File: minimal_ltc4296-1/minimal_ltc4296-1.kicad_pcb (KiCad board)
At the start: 2 copper layers, 15.2 x 15.2 mm, 1 part, among them U1 LTC4296AUK-1-PBF

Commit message: Update KiCad project files
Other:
- copper layers 2 -> 4
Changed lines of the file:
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@@
 	(layers
 		(0 "F.Cu" signal)
+		(4 "In1.Cu" power)
+		(6 "In2.Cu" power)
 		(2 "B.Cu" signal)
 		(9 "F.Adhes" user "F.Adhesive")
@@
 		(43 "User.3" user)
 		(45 "User.4" user)
+		(47 "User.5" user)
+		(49 "User.6" user)
+		(51 "User.7" user)
+		(53 "User.8" user)
+		(55 "User.9" user)
 	)
 	(setup
+		(stackup
+			(layer "F.SilkS"
+				(type "Top Silk Screen")
+				(color "White")
+				(material "Direct Printing")
+			)
+			(layer "F.Paste"
+				(type "Top Solder Paste")
+			)
+			(layer "F.Mask"
+				(type "Top Solder Mask")
+				(color "Green")
+				(thickness 0.01)
+				(material "Epoxy")
+				(epsilon_r 3.3)
+				(loss_tangent 0)
+			)
+			(layer "F.Cu"
+				(type "copper")
+				(thickness 0.035)
+			)
+			(layer "dielectric 1"
+				(type "prepreg")
+				(color "FR4 natural")
+				(thickness 0.1)
+				(material "FR4")
+				(epsilon_r 4.5)
+				(loss_tangent 0.02)
+			)
+			(layer "In1.Cu"
+				(type "copper")
+				(thickness 0.035)
+			)
+			(layer "dielectric 2"
+				(type "core")
+				(color "FR4 natural")
+				(thickness 1.24)
+				(material "FR4")
+				(epsilon_r 4.5)
+				(loss_tangent 0.02)
+			)
+			(layer "In2.Cu"
+				(type "copper")
+				(thickness 0.035)
+			)
+			(layer "dielectric 3"
+				(type "prepreg")
+				(color "FR4 natural")
+				(thickness 0.1)
+				(material "FR4")
+				(epsilon_r 4.5)
+				(loss_tangent 0.02)
+			)
+			(layer "B.Cu"
+				(type "copper")
+				(thickness 0.035)
+			)
+			(layer "B.Mask"
+				(type "Bottom Solder Mask")
+				(color "Green")
+				(thickness 0.01)
+				(material "Epoxy")
+				(epsilon_r 3.3)
+				(loss_tangent 0)
+			)
+			(layer "B.Paste"
+				(type "Bottom Solder Paste")
+			)
+			(layer "B.SilkS"
+				(type "Bottom Silk Screen")
+				(color "White")
+				(material "Direct Printing")
+			)
+			(copper_finish "Immersion gold")
+			(dielectric_constraints yes)
+			(edge_connector yes)
+		)
 		(pad_to_mask_clearance 0)
 		(allow_soldermask_bridges_in_footprints no)

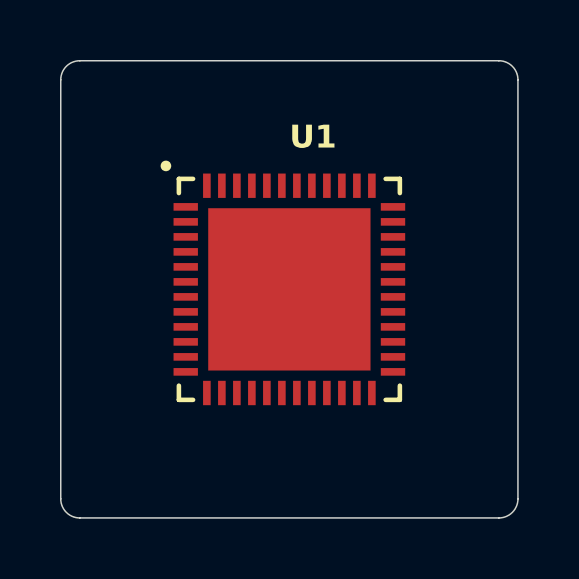
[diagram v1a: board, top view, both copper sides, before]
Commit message: Update KiCAD project files and generator
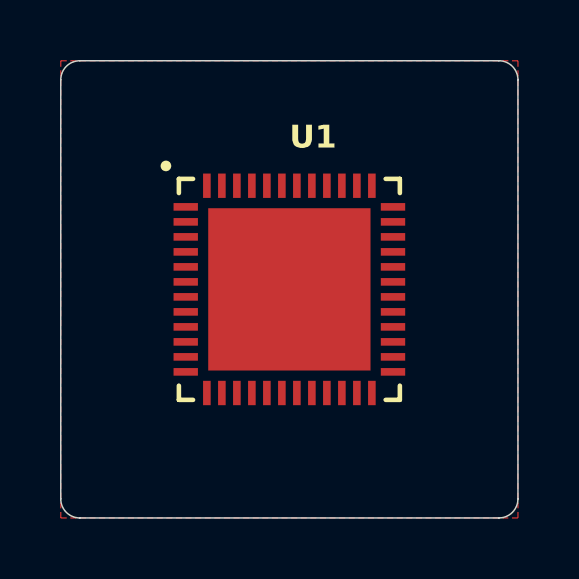
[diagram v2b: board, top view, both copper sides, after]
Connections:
- U1 pad 21: unconnected-(U1-GND-Pad21) -> GND
- U1 pad 24: unconnected-(U1-LSRC-Pad24) -> GND
- U1 pad 49: unconnected-(U1-GND-Pad49) -> GND
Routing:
- added copper zone on F.Cu, net GND
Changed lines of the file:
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@@
 	(net 11 "unconnected-(U1-LSNS1{slash}LSNS2-Pad28)")
 	(net 12 "unconnected-(U1-SW3-Pad19)")
-	(net 13 "unconnected-(U1-LSRC-Pad24)")
+	(net 13 "GND")
 	(net 14 "unconnected-(U1-HSNSP1-Pad48)")
 	(net 15 "unconnected-(U1-HSNSM2-Pad43)")
@@
 	(net 21 "unconnected-(U1-SW4-Pad20)")
 	(net 22 "unconnected-(U1-CPO-Pad7)")
-	(net 23 "unconnected-(U1-*CS-Pad12)")
+	(net 23 "unconnected-(U1-~{CS}-Pad12)")
 	(net 24 "unconnected-(U1-SW0-Pad16)")
 	(net 25 "unconnected-(U1-LSNS3{slash}LSNS4-Pad31)")
@@
 	(net 35 "unconnected-(U1-RT-Pad22)")
 	(net 36 "unconnected-(U1-OUTP0-Pad1)")
-	(net 37 "unconnected-(U1-GND-Pad49)")
-	(net 38 "unconnected-(U1-GND-Pad21)")
-	(net 39 "unconnected-(U1-HSNSM1-Pad47)")
-	(net 40 "unconnected-(U1-OUTP1-Pad45)")
-	(net 41 "unconnected-(U1-HGATE4-Pad34)")
-	(net 42 "unconnected-(U1-OUTM4-Pad32)")
-	(net 43 "unconnected-(U1-AUTO-Pad13)")
-	(net 44 "unconnected-(U1-SW2-Pad18)")
-	(net 45 "unconnected-(U1-HSNSM4-Pad35)")
-	(net 46 "unconnected-(U1-OUTM0-Pad25)")
-	(net 47 "unconnected-(U1-HSNSP2-Pad44)")
-	(net 48 "unconnected-(U1-HSNSM3-Pad39)")
-	(net 49 "unconnected-(U1-OUTP2-Pad41)")
+	(net 37 "unconnected-(U1-HSNSM1-Pad47)")
+	(net 38 "unconnected-(U1-OUTP1-Pad45)")
+	(net 39 "unconnected-(U1-HGATE4-Pad34)")
+	(net 40 "unconnected-(U1-OUTM4-Pad32)")
+	(net 41 "unconnected-(U1-AUTO-Pad13)")
+	(net 42 "unconnected-(U1-SW2-Pad18)")
+	(net 43 "unconnected-(U1-HSNSM4-Pad35)")
+	(net 44 "unconnected-(U1-OUTM0-Pad25)")
+	(net 45 "unconnected-(U1-HSNSP2-Pad44)")
+	(net 46 "unconnected-(U1-HSNSM3-Pad39)")
+	(net 47 "unconnected-(U1-OUTP2-Pad41)")
 	(footprint "analog_devices_footprints:QFN48_05-08-7073_ADI"
 		(layer "F.Cu")
@@
 			(size 0.254 0.8128)
 			(layers "F.Cu" "F.Mask" "F.Paste")
-			(net 23 "unconnected-(U1-*CS-Pad12)")
-			(pinfunction "*CS")
+			(net 23 "unconnected-(U1-~{CS}-Pad12)")
+			(pinfunction "~{CS}")
 			(pintype "input")
 		)
@@
 			(size 0.254 0.8128)
 			(layers "F.Cu" "F.Mask" "F.Paste")
-			(net 43 "unconnected-(U1-AUTO-Pad13)")
+			(net 41 "unconnected-(U1-AUTO-Pad13)")
 			(pinfunction "AUTO")
 			(pintype "unspecified")
@@
 			(size 0.254 0.8128)
 			(layers "F.Cu" "F.Mask" "F.Paste")
-			(net 44 "unconnected-(U1-SW2-Pad18)")
+			(net 42 "unconnected-(U1-SW2-Pad18)")
 			(pinfunction "SW2")
 			(pintype "output")
@@
 			(size 0.254 0.8128)
 			(layers "F.Cu" "F.Mask" "F.Paste")
-			(net 38 "unconnected-(U1-GND-Pad21)")
+			(net 13 "GND")
 			(pinfunction "GND")
 			(pintype "power_out")
@@
 			(size 0.254 0.8128)
 			(layers "F.Cu" "F.Mask" "F.Paste")
-			(net 13 "unconnected-(U1-LSRC-Pad24)")
+			(net 13 "GND")
 			(pinfunction "LSRC")
 			(pintype "unspecified")
@@
 			(size 0.254 0.8128)
 			(layers "F.Cu" "F.Mask" "F.Paste")
-			(net 46 "unconnected-(U1-OUTM0-Pad25)")
+			(net 44 "unconnected-(U1-OUTM0-Pad25)")
 			(pinfunction "OUTM0")
 			(pintype "output")
@@
 			(size 0.254 0.8128)
 			(layers "F.Cu" "F.Mask" "F.Paste")
-			(net 42 "unconnected-(U1-OUTM4-Pad32)")
+			(net 40 "unconnected-(U1-OUTM4-Pad32)")
 			(pinfunction "OUTM4")
 			(pintype "output")
@@
 			(size 0.254 0.8128)
 			(layers "F.Cu" "F.Mask" "F.Paste")
-			(net 41 "unconnected-(U1-HGATE4-Pad34)")
+			(net 39 "unconnected-(U1-HGATE4-Pad34)")
 			(pinfunction "HGATE4")
 			(pintype "unspecified")
@@
 			(size 0.254 0.8128)
 			(layers "F.Cu" "F.Mask" "F.Paste")
-			(net 45 "unconnected-(U1-HSNSM4-Pad35)")
+			(net 43 "unconnected-(U1-HSNSM4-Pad35)")
 			(pinfunction "HSNSM4")
 			(pintype "input")
@@
 			(size 0.254 0.8128)
 			(layers "F.Cu" "F.Mask" "F.Paste")
-			(net 48 "unconnected-(U1-HSNSM3-Pad39)")
+			(net 46 "unconnected-(U1-HSNSM3-Pad39)")
 			(pinfunction "HSNSM3")
 			(pintype "input")
@@
 			(size 0.254 0.8128)
 			(layers "F.Cu" "F.Mask" "F.Paste")
-			(net 49 "unconnected-(U1-OUTP2-Pad41)")
+			(net 47 "unconnected-(U1-OUTP2-Pad41)")
 			(pinfunction "OUTP2")
 			(pintype "output")
@@
 			(size 0.254 0.8128)
 			(layers "F.Cu" "F.Mask" "F.Paste")
-			(net 47 "unconnected-(U1-HSNSP2-Pad44)")
+			(net 45 "unconnected-(U1-HSNSP2-Pad44)")
 			(pinfunction "HSNSP2")
 			(pintype "input")
@@
 			(size 0.254 0.8128)
 			(layers "F.Cu" "F.Mask" "F.Paste")
-			(net 40 "unconnected-(U1-OUTP1-Pad45)")
+			(net 38 "unconnected-(U1-OUTP1-Pad45)")
 			(pinfunction "OUTP1")
 			(pintype "output")
@@
 			(size 0.254 0.8128)
 			(layers "F.Cu" "F.Mask" "F.Paste")
-			(net 39 "unconnected-(U1-HSNSM1-Pad47)")
+			(net 37 "unconnected-(U1-HSNSM1-Pad47)")
 			(pinfunction "HSNSM1")
 			(pintype "input")
@@
 			(size 5.4102 5.4102)
 			(layers "F.Cu" "F.Mask" "F.Paste")
-			(net 37 "unconnected-(U1-GND-Pad49)")
+			(net 13 "GND")
 			(pinfunction "GND")
 			(pintype "power_out")
+			(zone_connect 2)
 		)
 		(embedded_fonts no)
@@
 		(layer "Edge.Cuts")
 	)
+	(zone
+		(net 13)
+		(net_name "GND")
+		(layer "F.Cu")
+		(hatch none 0.508)
+		(connect_pads
+			(clearance 0.2032)
+		)
+		(min_thickness 0.2032)
+		(filled_areas_thickness no)
+		(fill yes
+			(thermal_gap 0.2032)
+			(thermal_bridge_width 0.2032)
+			(smoothing fillet)
+			(radius 0.508)
+		)
+		(polygon
+			(pts
+				(xy 142.0876 94.742) (xy 142.0876 109.982) (xy 157.3276 109.982) (xy 157.3276 94.742)
+			)
+		)
+	)
 	(embedded_fonts no)

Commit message: Update KiCad project files
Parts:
- added C1: 1 nF, capacitor_footprints:C_0402_1005Metric, F.Cu at (144.8, 102.4)
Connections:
- U1 pad 6: unconnected-(U1-IN-Pad6) -> /IN
- U1 pad 7: unconnected-(U1-CPO-Pad7) -> /CPO
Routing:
- net /IN: track 0.00 -> 1.49 mm
- net /CPO: track 0.00 -> 1.49 mm

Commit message: Update KiCAD files and submodule
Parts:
- added C2: 100 nF, capacitor_footprints:C_0603_1608Metric, F.Cu at (143.4, 99.5)
- added C3: 10 µF, capacitor_footprints:C_1210_250_3225Metric, F.Cu at (140.9, 102.0)
- added C4: 470 nF, capacitor_footprints:C_0402_1005Metric, F.Cu at (143.4, 104.2)
- added C5: 100 nF, capacitor_footprints:C_0603_1608Metric, F.Cu at (138.9, 108.6)
- added D1: 58 V, diode_footprints:DO-214AA, F.Cu at (137.0, 103.0)
- added R1: 10 kΩ, resistor_footprints:R_0402_1005Metric, F.Cu at (142.0, 105.9)
- added R2: 4.99 kΩ, resistor_footprints:R_0402_1005Metric, F.Cu at (142.0, 107.2)
- added R3: 10 kΩ, resistor_footprints:R_0402_1005Metric, F.Cu at (142.0, 108.6)
- added R4: 10 kΩ, resistor_footprints:R_0402_1005Metric, F.Cu at (145.4, 108.6)
- moved C1 1.42 mm to (143.4, 102.1)
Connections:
- U1 pad 10: unconnected-(U1-SDO-Pad10) -> /SDO
- U1 pad 11: unconnected-(U1-SCK-Pad11) -> /SCK
- U1 pad 12: unconnected-(U1-~{CS}-Pad12) -> /~{CS}
- U1 pad 8: unconnected-(U1-INT-Pad8) -> /INT
- U1 pad 9: unconnected-(U1-SDI-Pad9) -> /SDI
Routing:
- net /SCK: track 0.00 -> 6.48 mm, vias 0 -> 2
- net /SDO: track 0.00 -> 5.79 mm, vias 0 -> 2
- net /~{CS}: track 0.00 -> 5.54 mm, vias 0 -> 2
- net /SDI: track 0.00 -> 5.16 mm, vias 0 -> 2
- net /INT: track 0.00 -> 2.96 mm
- net /IN: track 1.49 -> 0.00 mm, vias 0 -> 8
- net /CPO: track 1.49 -> 2.82 mm
- net GND: vias 0 -> 9
- net /3V3: vias 0 -> 5
- added copper zone on F.Cu, net /3V3
- added copper zone on F.Cu, net /IN
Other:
- board size 15.2 x 15.2 mm -> 25.4 x 17.8 mm

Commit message: Update KiCAD files and submodule
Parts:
- added R5: 100 kΩ, resistor_footprints:R_0402_1005Metric, F.Cu at (147.2, 109.7)
- added R6: 100 kΩ, resistor_footprints:R_0402_1005Metric, F.Cu at (148.6, 109.7)
- moved R1 3.79 mm to (142.0, 109.7), turned to 90 degrees
- moved R3 2.80 mm to (144.6, 109.7), turned to 90 degrees
- moved R2 2.76 mm to (143.3, 109.7), turned to 90 degrees
- moved C5 1.91 mm to (140.4, 109.7), turned to 90 degrees
- moved R4 1.29 mm to (145.9, 109.7), turned to 90 degrees
- moved D1 0.25 mm to (136.8, 103.0)
- moved C3 0.25 mm to (140.6, 102.0)
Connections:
- U1 pad 13: unconnected-(U1-AUTO-Pad13) -> /AUTO
- U1 pad 14: unconnected-(U1-WAKEUP-Pad14) -> /WAKEUP
- U1 pad 16: unconnected-(U1-SW0-Pad16) -> /SW0
- U1 pad 17: unconnected-(U1-SW1-Pad17) -> /SW1
- U1 pad 18: unconnected-(U1-SW2-Pad18) -> /SW2
- U1 pad 19: unconnected-(U1-SW3-Pad19) -> /SW3
- U1 pad 20: unconnected-(U1-SW4-Pad20) -> /SW4
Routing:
- net /AUTO: track 0.00 -> 4.91 mm, vias 0 -> 2
- net /SDI: track 5.16 -> 8.24 mm
- net /SW2: track 0.00 -> 2.16 mm, vias 0 -> 1
- net /SW3: track 0.00 -> 1.67 mm, vias 0 -> 1
- net /SW1: track 0.00 -> 1.67 mm, vias 0 -> 1
- net /SDO: track 5.79 -> 7.01 mm
- net /SW0: track 0.00 -> 1.17 mm, vias 0 -> 1
- net /WAKEUP: track 0.00 -> 1.17 mm, vias 0 -> 1
- net /SW4: track 0.00 -> 1.17 mm, vias 0 -> 1
- net /SCK: track 6.48 -> 5.82 mm
- net GND: vias 9 -> 10
- net /3V3: vias 5 -> 6
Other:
- board size 25.4 x 17.8 mm -> 25.4 x 20.3 mm

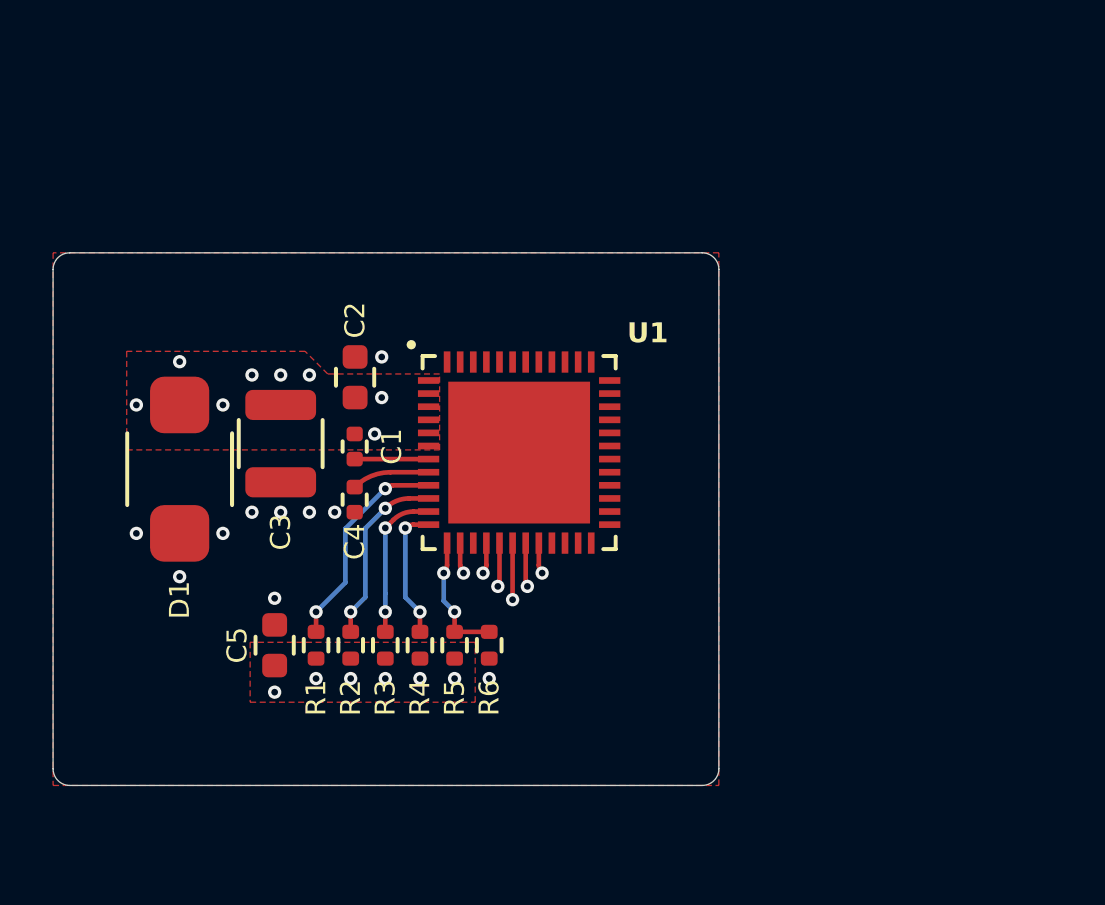
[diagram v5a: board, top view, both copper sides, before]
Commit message: Update KiCAD project files and generator
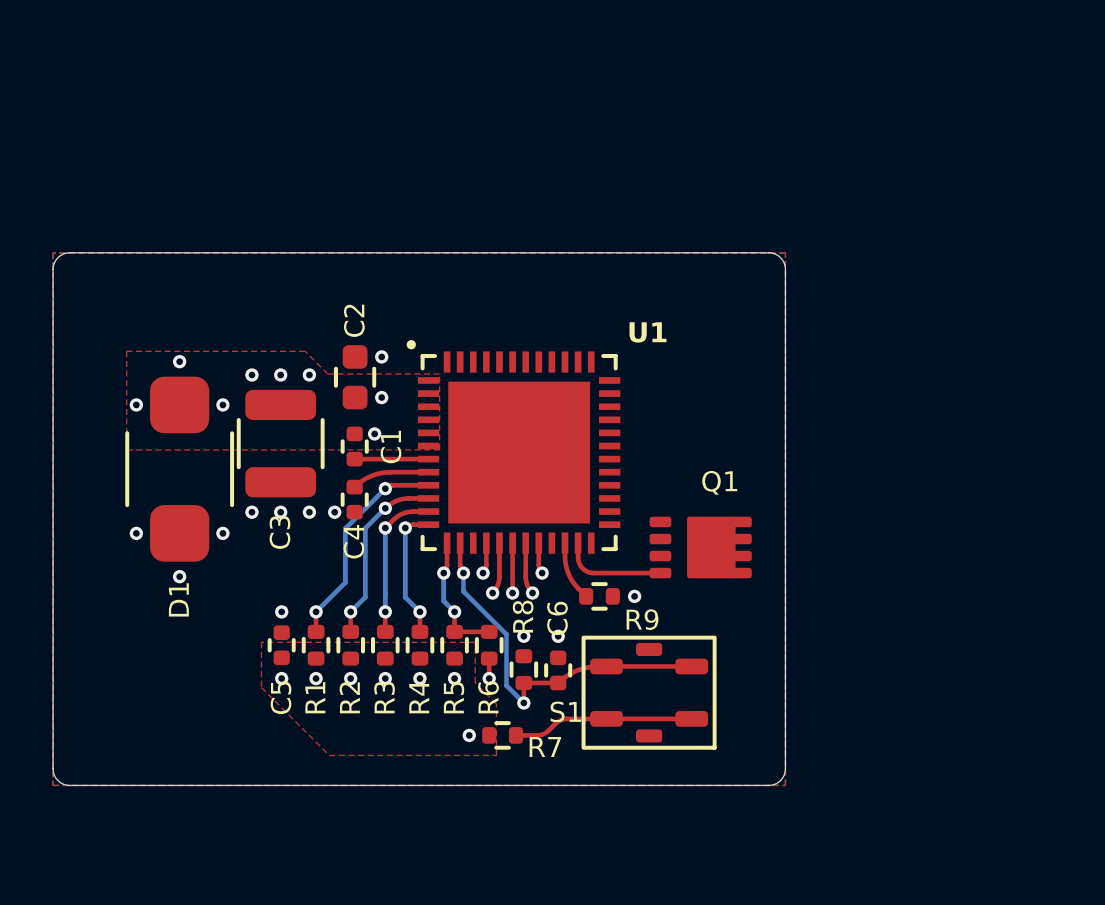
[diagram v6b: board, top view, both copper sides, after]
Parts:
- added C6: 1 nF, capacitor_footprints:C_0402_1005Metric, F.Cu at (151.2, 110.7)
- added Q1: 100.0 V, transistor_footprints:LFPAK33-8, F.Cu at (156.6, 106.0)
- added R7: 1 kΩ, resistor_footprints:R_0402_1005Metric, F.Cu at (149.1, 113.2)
- added R8: 100 kΩ, resistor_footprints:R_0402_1005Metric, F.Cu at (149.9, 110.6)
- added R9: 24.3 kΩ, resistor_footprints:R_0402_1005Metric, F.Cu at (152.8, 107.8)
- added S1: TS21-34-035-BK-160-SMT-TR, tactile_switches_footprints:TS21, F.Cu at (154.7, 111.5)
- C5: value 100 nF -> 1 nF; footprint capacitor_footprints:C_0603_1608Metric -> capacitor_footprints:C_0402_1005Metric
- moved C5 0.27 mm to (140.6, 109.7)
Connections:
- U1 pad 22: unconnected-(U1-RT-Pad22) -> /RT
- U1 pad 23: unconnected-(U1-LGATE-Pad23) -> Net-(Q1-G)
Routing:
- net /WAKEUP: track 1.17 -> 14.4 mm, vias 1 -> 2
- net Net-(R7-Pad2): track 0.00 -> 6.90 mm
- net Net-(Q1-G): track 0.00 -> 4.00 mm
- net /RT: track 0.00 -> 2.28 mm
- net GND: track 0.00 -> 0.76 mm, vias 10 -> 13
- net /3V3: vias 6 -> 7
- added copper zone on In1.Cu, net /3V3
- added copper zone on In1.Cu, net /IN
- added copper zone on B.Cu, net GND
- added copper zone on In1.Cu, net GND
- added copper zone on In2.Cu, net GND
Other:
- board size 25.4 x 20.3 mm -> 27.9 x 20.3 mm

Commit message: Update KiCAD schematic and PCB files
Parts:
- added R10: 24 mΩ, resistor_footprints:R_0612_1632Metric, F.Cu at (163.1, 101.2)
- added R11: 62 mΩ, resistor_footprints:R_0612_1632Metric, F.Cu at (163.1, 97.8)
- added R12: 16 mΩ, resistor_footprints:R_0612_1632Metric, F.Cu at (163.1, 107.9)
- added R13: 62 mΩ, resistor_footprints:R_0612_1632Metric, F.Cu at (163.1, 104.5)
- added R14: 390 mΩ, resistor_footprints:R_0612_1632Metric, F.Cu at (163.1, 111.2)
- moved Q1 2.08 mm to (156.1, 108.0)
- moved R9 0.73 mm to (152.2, 108.2), turned to -90 degrees
- moved S1 0.63 mm to (154.7, 112.2)
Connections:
- Q1 pad 5: unconnected-(Q1-D-Pad5) -> /LSNS
- U1 pad 25: unconnected-(U1-OUTM0-Pad25) -> /OUTM0
- U1 pad 26: unconnected-(U1-LSNS0-Pad26) -> /LSNS
- U1 pad 27: unconnected-(U1-OUTM1-Pad27) -> /OUTM1
- U1 pad 28: unconnected-(U1-LSNS1/LSNS2-Pad28) -> /LSNS
- U1 pad 29: unconnected-(U1-OUTM2-Pad29) -> /OUTM2
- U1 pad 30: unconnected-(U1-OUTM3-Pad30) -> /OUTM3
- U1 pad 31: unconnected-(U1-LSNS3/LSNS4-Pad31) -> /LSNS
- U1 pad 32: unconnected-(U1-OUTM4-Pad32) -> /OUTM4
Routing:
- net /LSNS: track 0.00 -> 28.9 mm, vias 0 -> 6
- net /OUTM0: track 0.00 -> 11.0 mm, vias 0 -> 2
- net /OUTM1: track 0.00 -> 9.98 mm, vias 0 -> 2
- net /OUTM4: track 0.00 -> 9.98 mm, vias 0 -> 2
- net /OUTM3: track 0.00 -> 9.97 mm, vias 0 -> 2
- net /OUTM2: track 0.00 -> 9.89 mm, vias 0 -> 2
- net Net-(Q1-G): track 4.00 -> 4.78 mm
- added copper zone on F.Cu, net /LSNS
- added copper zone on In1.Cu, net /LSNS
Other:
- board size 27.9 x 20.3 mm -> 38.1 x 20.3 mm

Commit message: Update PCB and schematic files
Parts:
- added Q2: 100.0 V, transistor_footprints:LFPAK33-8, F.Cu at (154.5, 91.9)
- added Q3: 100.0 V, transistor_footprints:LFPAK33-8, F.Cu at (149.4, 91.9)
- added R15: 24 mΩ, resistor_footprints:R_0612_1632Metric, F.Cu at (154.3, 95.5)
- added R16: 390 mΩ, resistor_footprints:R_0612_1632Metric, F.Cu at (149.2, 95.5)
- moved R14 4.91 mm to (158.8, 113.6), turned to 0 degrees
- moved R11 4.52 mm to (158.8, 96.4), turned to 0 degrees
- moved R12 4.52 mm to (158.8, 109.3), turned to 0 degrees
- moved R10 4.32 mm to (158.8, 100.7), turned to 0 degrees
- moved R13 4.32 mm to (158.8, 105.0), turned to 0 degrees
- moved S1 2.91 mm to (152.8, 114.4)
- moved Q1 2.12 mm to (154.7, 109.5), turned to -90 degrees
- moved C6 0.34 mm to (151.2, 111.0)
- moved R8 0.34 mm to (149.9, 111.0)
- moved R7 0.34 mm to (149.1, 113.5)
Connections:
- C1 pad 1: /IN -> /PSE
- C2 pad 1: /IN -> /PSE
- C3 pad 1: /IN -> /PSE
- D1 pad 1: /IN -> /PSE
- U1 pad 33: unconnected-(U1-OUTP4-Pad33) -> /OUTP4
- U1 pad 34: unconnected-(U1-HGATE4-Pad34) -> /HGATE4
- U1 pad 35: unconnected-(U1-HSNSM4-Pad35) -> /HSNSM4
- U1 pad 36: unconnected-(U1-HSNSP4-Pad36) -> /PSE
- U1 pad 37: unconnected-(U1-OUTP3-Pad37) -> /OUTP3
- U1 pad 38: unconnected-(U1-HGATE3-Pad38) -> /HGATE3
- U1 pad 39: unconnected-(U1-HSNSM3-Pad39) -> /HSNSM3
- U1 pad 40: unconnected-(U1-HSNSP3-Pad40) -> /PSE
- U1 pad 6: /IN -> /PSE
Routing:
- net /LSNS: track 28.9 -> 23.8 mm
- net /PSE: track 0.00 -> 3.73 mm, vias 0 -> 9
- net /HSNSM4: track 0.00 -> 3.11 mm, vias 0 -> 1
- net /HGATE4: track 0.00 -> 3.00 mm, vias 0 -> 1
- net /OUTP4: track 0.00 -> 2.89 mm, vias 0 -> 1
- net Net-(Q1-G): track 4.78 -> 3.39 mm
- net /OUTM0: track 11.0 -> 12.3 mm
- net /OUTM3: track 9.97 -> 8.93 mm
- net /OUTM2: track 9.89 -> 8.93 mm
- net GND: track 0.76 -> 0.00 mm
- net /OUTM4: track 9.98 -> 9.31 mm
- net /OUTM1: track 9.98 -> 9.34 mm
- net /IN: vias 8 -> 0
- added copper zone on F.Cu, net /OUTM0
- added copper zone on F.Cu, net /OUTM1
- added copper zone on F.Cu, net /OUTM2
- added copper zone on F.Cu, net /OUTM3
- added copper zone on F.Cu, net /OUTM4
- added copper zone on F.Cu, net /PSE
- added copper zone on In1.Cu, net /PSE
- removed copper zone on F.Cu, net /IN
- removed copper zone on In1.Cu, net /IN
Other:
- board size 38.1 x 20.3 mm -> 38.1 x 30.5 mm
